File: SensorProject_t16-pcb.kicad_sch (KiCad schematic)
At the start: 51 parts, among them J1 Conn_01x02_Pin, J10 Conn_01x02_Pin, J11 Conn_01x02_Pin, J12 Conn_01x02_Pin, J13 Conn_01x02_Pin, J14 Conn_01x02_Pin, J15 Conn_01x02_Pin, J16 Conn_01x02_Pin, J17 Conn_01x04_Socket, J2 Conn_01x02_Pin, J3 Conn_01x02_Pin, J4 Conn_01x02_Pin, J5 Conn_01x02_Pin, J6 Conn_01x02_Pin, J7 Conn_01x02_Pin, J8 Conn_01x02_Pin, J9 Conn_01x02_Pin, U1 ADS1115IDGS, U2 ADS1115IDGS, U3 ADS1115IDGS, U4 ADS1115IDGS

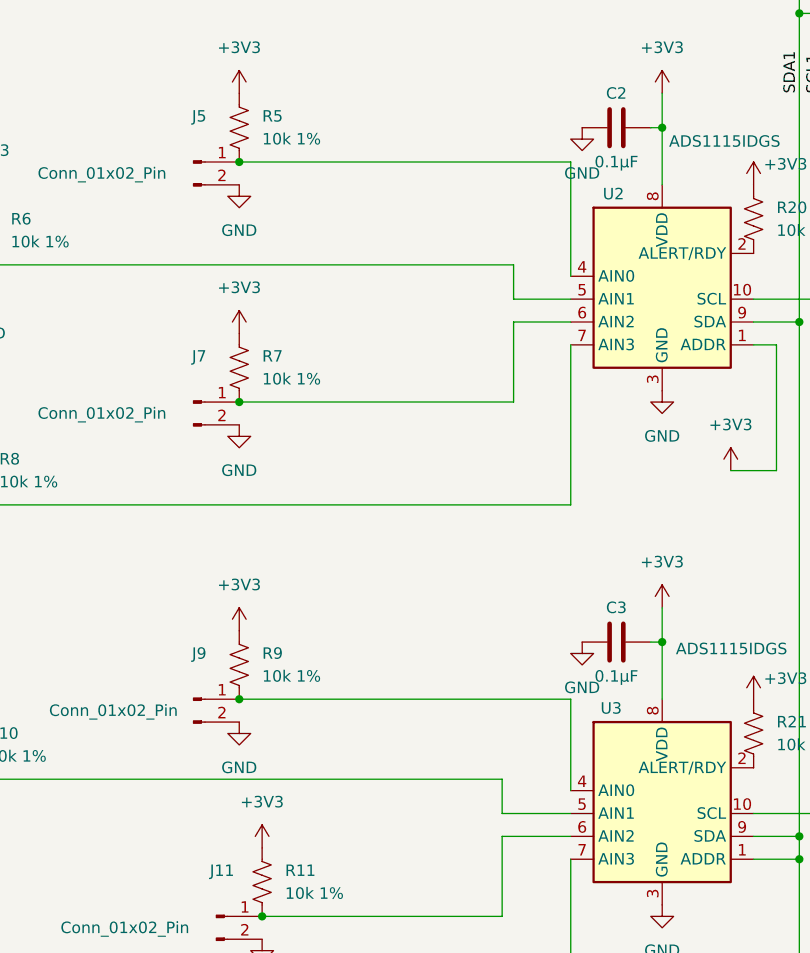
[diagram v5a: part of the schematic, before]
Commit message: layout with F411 roughly good but needs work.
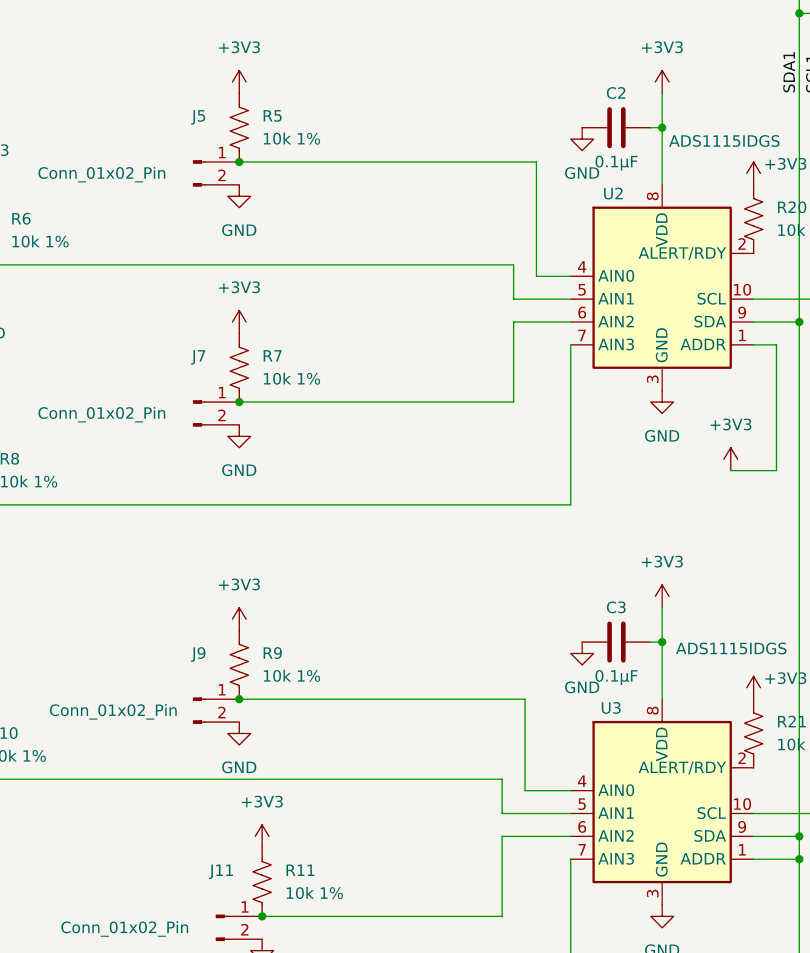
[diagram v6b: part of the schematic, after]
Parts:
- C1, C2, C3, C4: footprint ProjectLib:C_0805_2012Metric -> ProjectLib:C_0603_1608Metric
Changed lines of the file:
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@@
 	(wire
 		(pts
+			(xy 111.76 101.6) (xy 115.57 101.6)
+		)
+		(stroke
+			(width 0)
+			(type default)
+		)
+	)
+	(wire
+		(pts
 			(xy 115.57 184.15) (xy 115.57 166.37)
 		)
@@
 	(wire
 		(pts
+			(xy 110.49 158.75) (xy 115.57 158.75)
+		)
+		(stroke
+			(width 0)
+			(type default)
+		)
+	)
+	(wire
+		(pts
 			(xy 105.41 45.72) (xy 115.57 45.72)
 		)
@@
 	(wire
 		(pts
-			(xy 78.74 148.59) (xy 115.57 148.59)
+			(xy 78.74 148.59) (xy 110.49 148.59)
 		)
 		(stroke
@@
 	(wire
 		(pts
-			(xy 115.57 148.59) (xy 115.57 158.75)
+			(xy 110.49 148.59) (xy 110.49 158.75)
 		)
 		(stroke
@@
 	(wire
 		(pts
-			(xy 115.57 101.6) (xy 115.57 88.9)
+			(xy 111.76 101.6) (xy 111.76 88.9)
 		)
 		(stroke
@@
 	(wire
 		(pts
-			(xy 78.74 88.9) (xy 115.57 88.9)
+			(xy 78.74 88.9) (xy 111.76 88.9)
 		)
 		(stroke
@@
 			)
 		)
-		(property "Footprint" "ProjectLib:C_0805_2012Metric"
+		(property "Footprint" "ProjectLib:C_0603_1608Metric"
 			(at 116.84 84.1248 0)
 			(effects
@@
 			)
 		)
-		(property "Footprint" "ProjectLib:C_0805_2012Metric"
+		(property "Footprint" "ProjectLib:C_0603_1608Metric"
 			(at 116.84 23.1648 0)
 			(effects
@@
 			)
 		)
-		(property "Footprint" "ProjectLib:C_0805_2012Metric"
+		(property "Footprint" "ProjectLib:C_0603_1608Metric"
 			(at 119.38 195.8848 0)
 			(effects
@@
 			)
 		)
-		(property "Footprint" "ProjectLib:C_0805_2012Metric"
+		(property "Footprint" "ProjectLib:C_0603_1608Metric"
 			(at 116.84 141.2748 0)
 			(effects

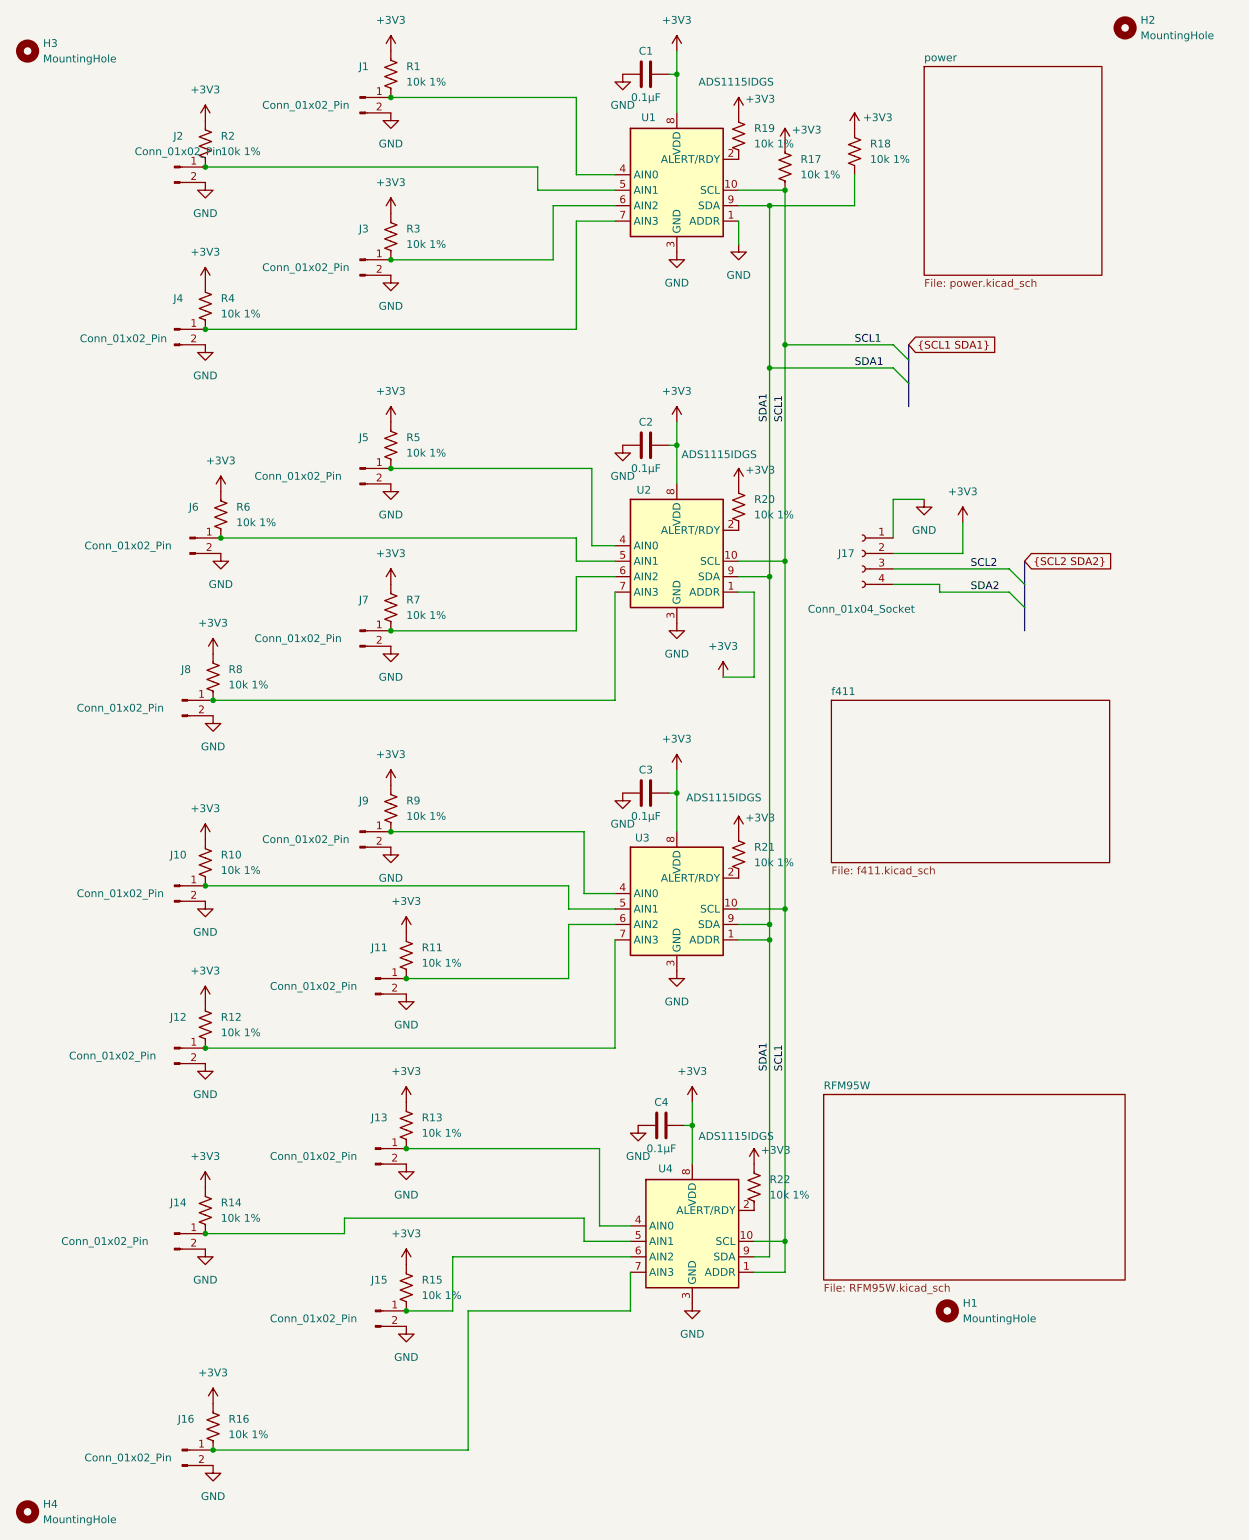
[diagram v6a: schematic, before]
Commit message: near complete, DRC good, ERC has a spurious error about ground on Y1.
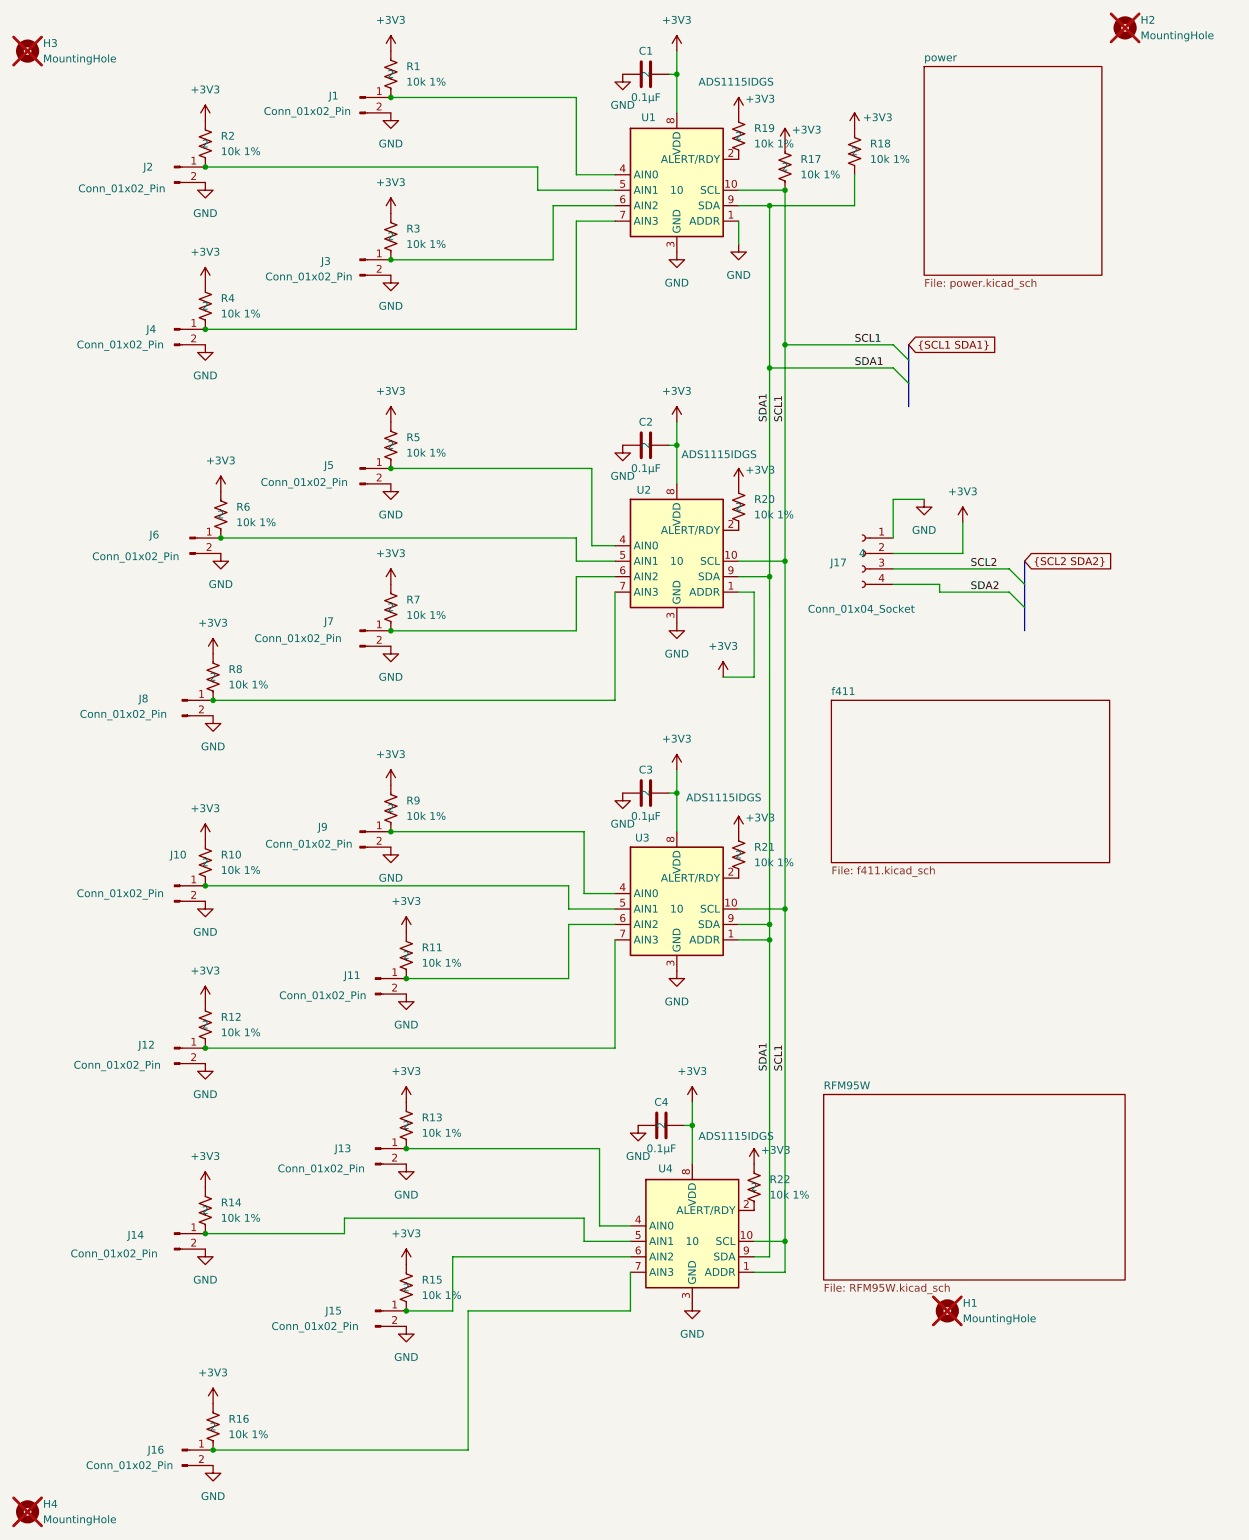
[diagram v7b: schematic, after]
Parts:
- C1, C2, C3, C4, R1, R10, R11, R12, R13, R14, R15, R16, R17, R18, R19, R2, R20, R21, R22, R3, R4, R5, R6, R7, R8, R9: pads (none) -> 2
- H1, H2, H3, H4: now not fitted; now left out of the parts list
- J1, J10, J11, J12, J13, J14, J15, J16, J2, J3, J4, J5, J6, J7, J8, J9: Manufacturer (none) -> JST; MfgPart (none) -> B2B-XH-A; Notes (none) -> or equivalent; pads (none) -> 2
- J17: Manufacturer (none) -> JILN; MfgPart (none) -> 22850104ANG1SYA01; Notes (none) -> or equivalent; pads (none) -> 4
- U1, U2, U3, U4: pads (none) -> 10

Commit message: cleanup, ready to submit.
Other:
- moved on the sheet: R19, R20, R21, R22
